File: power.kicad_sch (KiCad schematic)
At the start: 80 parts, among them IC1 STM32MP157AAB3, IC3 STC3117IJT, IC4 MCP73830T-2AAI_MYY, IC5 MT41K256M16TW-107_P, IC6 STPMIC1BPQR, IC8 STUSB1600AQTR, J1 Conn_01x04, P1 USB_C_Plug_USB2.0, Q1 PMDPB70XP_115

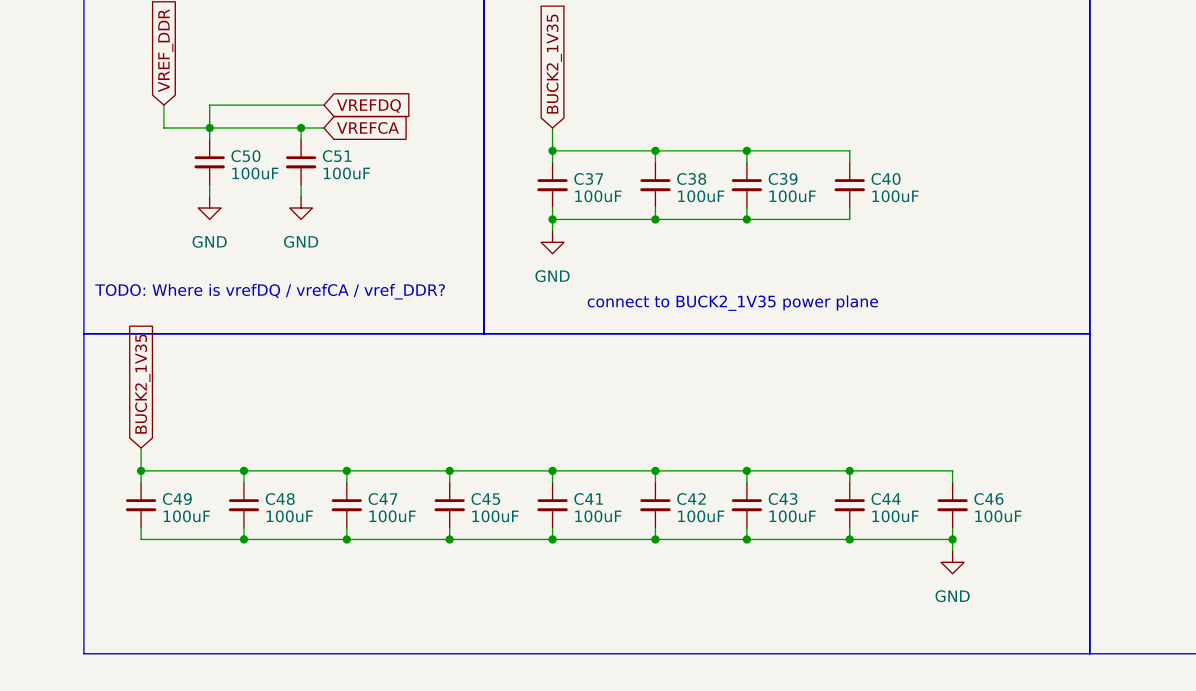
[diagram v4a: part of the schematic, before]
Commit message: added supply to nRF
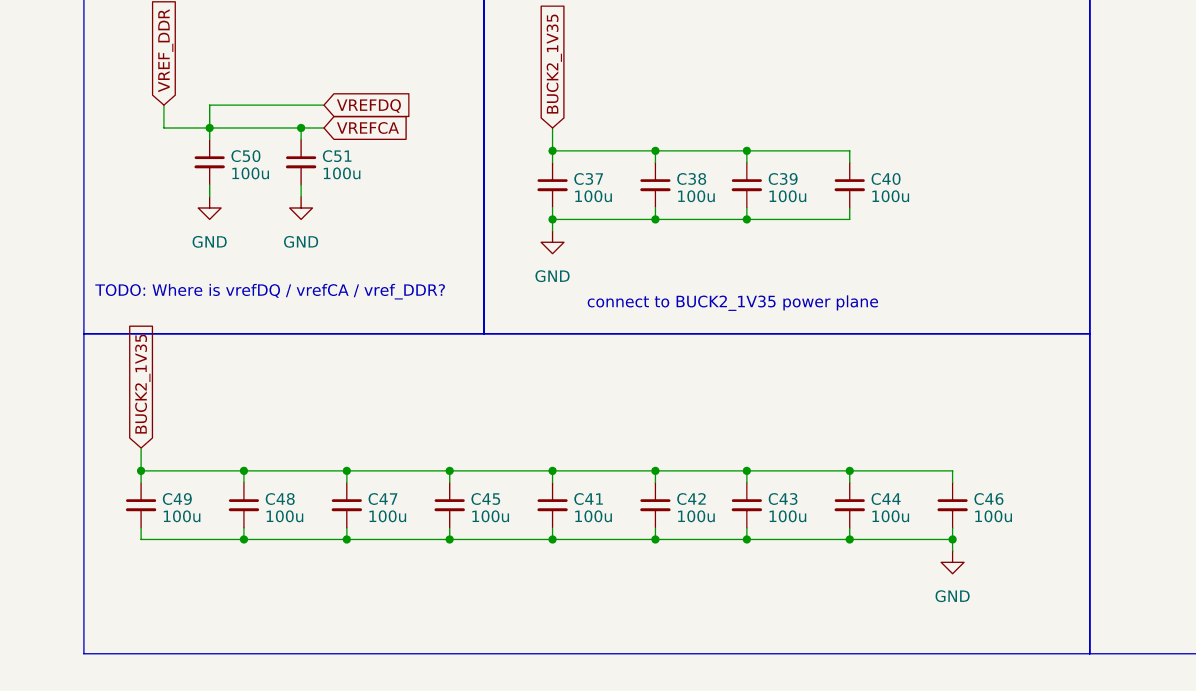
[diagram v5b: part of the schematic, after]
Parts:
- C37, C38, C39, C40, C41, C42, C43, C44, C45, C46, C47, C48, C49, C50, C51: value 100uF -> 100u
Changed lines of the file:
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@@
       (effects (font (size 1.27 1.27)) (justify left))
     )
-    (property "Value" "100uF" (at 232.1941 238.7736 0)
+    (property "Value" "100u" (at 232.1941 238.7736 0)
       (effects (font (size 1.27 1.27)) (justify left))
     )
@@
       (effects (font (size 1.27 1.27)) (justify left))
     )
-    (property "Value" "100uF" (at 220.7641 238.7736 0)
+    (property "Value" "100u" (at 220.7641 238.7736 0)
       (effects (font (size 1.27 1.27)) (justify left))
     )
@@
       (effects (font (size 1.27 1.27)) (justify left))
     )
-    (property "Value" "100uF" (at 186.4741 238.7736 0)
+    (property "Value" "100u" (at 186.4741 238.7736 0)
       (effects (font (size 1.27 1.27)) (justify left))
     )
@@
       (effects (font (size 1.27 1.27)) (justify left))
     )
-    (property "Value" "100uF" (at 253.7841 203.2136 0)
+    (property "Value" "100u" (at 253.7841 203.2136 0)
       (effects (font (size 1.27 1.27)) (justify left))
     )
@@
       (effects (font (size 1.27 1.27)) (justify left))
     )
-    (property "Value" "100uF" (at 197.9041 238.7736 0)
+    (property "Value" "100u" (at 197.9041 238.7736 0)
       (effects (font (size 1.27 1.27)) (justify left))
     )
@@
       (effects (font (size 1.27 1.27)) (justify left))
     )
-    (property "Value" "100uF" (at 243.6241 238.7736 0)
+    (property "Value" "100u" (at 243.6241 238.7736 0)
       (effects (font (size 1.27 1.27)) (justify left))
     )
@@
       (effects (font (size 1.27 1.27)) (justify left))
     )
-    (property "Value" "100uF" (at 194.0941 200.6736 0)
+    (property "Value" "100u" (at 194.0941 200.6736 0)
       (effects (font (size 1.27 1.27)) (justify left))
     )
@@
       (effects (font (size 1.27 1.27)) (justify left))
     )
-    (property "Value" "100uF" (at 265.2141 238.7736 0)
+    (property "Value" "100u" (at 265.2141 238.7736 0)
       (effects (font (size 1.27 1.27)) (justify left))
     )
@@
       (effects (font (size 1.27 1.27)) (justify left))
     )
-    (property "Value" "100uF" (at 276.6441 238.7736 0)
+    (property "Value" "100u" (at 276.6441 238.7736 0)
       (effects (font (size 1.27 1.27)) (justify left))
     )
@@
       (effects (font (size 1.27 1.27)) (justify left))
     )
-    (property "Value" "100uF" (at 209.3341 238.7736 0)
+    (property "Value" "100u" (at 209.3341 238.7736 0)
       (effects (font (size 1.27 1.27)) (justify left))
     )
@@
       (effects (font (size 1.27 1.27)) (justify left))
     )
-    (property "Value" "100uF" (at 265.2141 203.2136 0)
+    (property "Value" "100u" (at 265.2141 203.2136 0)
       (effects (font (size 1.27 1.27)) (justify left))
     )
@@
       (effects (font (size 1.27 1.27)) (justify left))
     )
-    (property "Value" "100uF" (at 253.7841 238.7736 0)
+    (property "Value" "100u" (at 253.7841 238.7736 0)
       (effects (font (size 1.27 1.27)) (justify left))
     )
@@
       (effects (font (size 1.27 1.27)) (justify left))
     )
-    (property "Value" "100uF" (at 243.6241 203.2136 0)
+    (property "Value" "100u" (at 243.6241 203.2136 0)
       (effects (font (size 1.27 1.27)) (justify left))
     )
@@
       (effects (font (size 1.27 1.27)) (justify left))
     )
-    (property "Value" "100uF" (at 204.2541 200.6736 0)
+    (property "Value" "100u" (at 204.2541 200.6736 0)
       (effects (font (size 1.27 1.27)) (justify left))
     )
@@
       (effects (font (size 1.27 1.27)) (justify left))
     )
-    (property "Value" "100uF" (at 232.1941 203.2136 0)
+    (property "Value" "100u" (at 232.1941 203.2136 0)
       (effects (font (size 1.27 1.27)) (justify left))
     )

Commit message: added decoupling capacitors to mp1
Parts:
- added C100, C101, C102, C103, C104, C105, C108, C110, C111, C115, C78, C79, C80, C81, C82, C83, C84, C85, C86, C87, C88, C89, C90, C91, C92, C93, C94, C95, C96, C99: 1u, Capacitor_SMD:C_0603_1608Metric, symbol Device:C_Small
- added C106, C107, C109: 2u2, Capacitor_SMD:C_0603_1608Metric, symbol Device:C_Small
- added C112, C116, C77: 100n, Capacitor_SMD:C_0603_1608Metric, symbol Device:C_Small
- added C97, C98: 1n, Capacitor_SMD:C_0603_1608Metric, symbol Device:C_Small
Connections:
- net BUCK1_1V2: now also C78.1, C79.1, C80.1, C81.1, C82.1, C83.1, C84.1, C85.1, C86.1, C87.1, C88.1, C89.1, C90.1, C91.1, C92.1; no longer IC1.B16 (VDD_1V2_DSI__REG)
- net BUCK2_1V35: now also C93.1, C94.1, C95.1, C96.1, C97.1, C98.1
- net BUCK4_1V8: now also C100.1, C101.1, C102.1, C103.1, C104.1, C105.1, C111.1, C112.1, C115.1, C116.1, C77.1, C99.1
- net GND: now also C100.2, C101.2, C102.2, C103.2, C104.2, C105.2, C106.2, C107.2, C108.2, C109.2, C110.2, C111.2, C112.2, C115.2, C116.2, C77.2, C78.2, C79.2, C80.2, C81.2, C82.2, C83.2, C84.2, C85.2, C86.2, C87.2, C88.2, C89.2, C90.2, C91.2, C92.2, C93.2, C94.2, C95.2, C96.2, C97.2, C98.2, C99.2
- net LDO1_1V8: now also C107.1, C108.1
- net VDD_USB renamed MP1_VDD_USB
- net MP1_VDD_USB: now also C110.1
- new net MP1_VDD1V2_DSI: C106.1, IC1.A16 (VDD1V2__DSI_PHY), IC1.B16 (VDD_1V2_DSI__REG)
- new net MP1_VDDA_1V1_REG: C109.1, IC1.W11 (VDDA_1V1_REG)
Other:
- note added: "RAM"
- note added: "VBAT"
- note added: "VDD"
- note added: "VDD1V2"
- note added: "VDDA"
- note added: "VDDA_1V1"
- note added: "VDDA_1V8"
- note added: "VDDQ_DDR"
- note added: "VDD_ANA"
- note added: "VDD_CORE"
- note added: "VDD_PLL"
- note added: "VDD_USB"
- note added: "VREF"
- note added: "VREF- must be connected to VSSA then to VSS plane"
- note added: "connect close to VSSA"
- note added: "connect close to VSSA and VREF-"
- note added: "connect close to VSS_ANA"
- note added: "connect close to VSS_PLL, VSS_PLL2"
- note added: "connect close to VSS_USBHS"
- note removed: "Caution: Datasheet P. 123 "Each power supply pair (VDD /VSS , VDDCORE/VSS, VDDA/VSSA ...) must be decoupled with filtering ceramic capacitors. These capacitors must be placed as close as possible to, or below, the appropriate pins on the underside of the PCB to ensure good operation of the device.""
- note removed: "VREF- == VSSA (== VSS?) Otherwise all GNDs can be linked together"
- moved on the sheet: C37, C38, C39, C40, C41, C42, C43, C44, C45, C46, C47, C48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

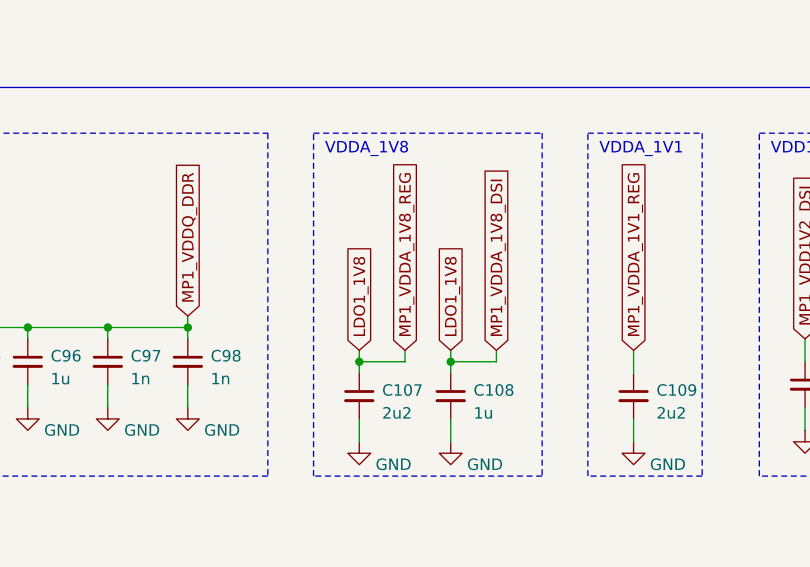
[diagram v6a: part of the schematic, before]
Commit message: fixed MP1_VDDA_1V8_REG connection
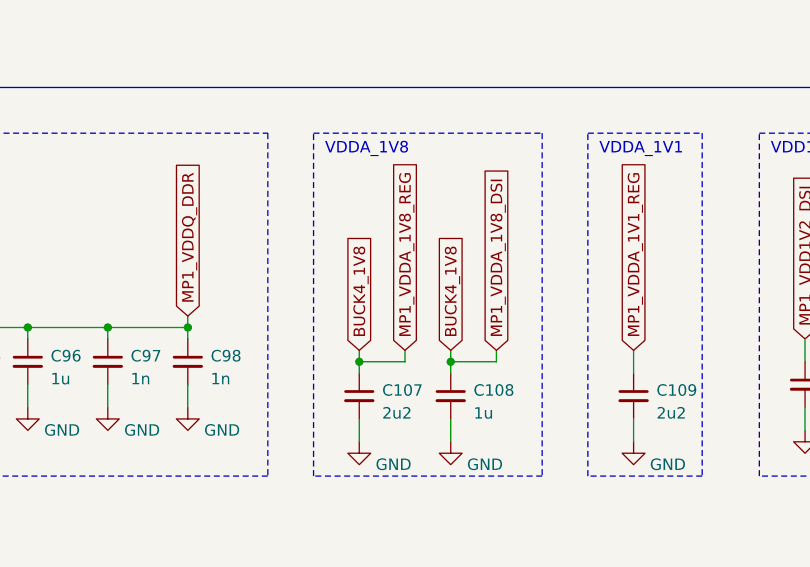
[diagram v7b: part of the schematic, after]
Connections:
- net LDO1_1V8 is gone; now on net BUCK4_1V8: C107.1, C108.1, IC1.B12 (VDDA_1V8_DSI), IC1.V11 (VDDA_1V8_REG)
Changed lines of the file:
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@@
+    )
+  )
+  (global_label "BUCK4_1V8" (shape input) (at 398.78 207.01 90) (fields_autoplaced)
+    (effects (font (size 1.27 1.27)) (justify left))
+    (property "Intersheetrefs" "${INTERSHEET_REFS}" (at 398.78 200.5966 90)
+      (effects (font (size 1.27 1.27)) (justify left) hide)
     )
   )
@@
     )
   )
-  (global_label "LDO1_1V8" (shape input) (at 398.78 207.01 90) (fields_autoplaced)
-    (effects (font (size 1.27 1.27)) (justify left))
-    (property "Intersheetrefs" "${INTERSHEET_REFS}" (at 398.78 194.7909 90)
-      (effects (font (size 1.27 1.27)) (justify left) hide)
-    )
-  )
   (global_label "SDA" (shape input) (at 280.67 111.76 180) (fields_autoplaced)
     (effects (font (size 1.27 1.27)) (justify right))
@@
     )
   )
+  (global_label "BUCK4_1V8" (shape input) (at 408.94 207.01 90) (fields_autoplaced)
+    (effects (font (size 1.27 1.27)) (justify left))
+    (property "Intersheetrefs" "${INTERSHEET_REFS}" (at 408.94 200.5966 90)
+      (effects (font (size 1.27 1.27)) (justify left) hide)
+    )
+  )
   (global_label "USB_ATTACH" (shape input) (at 176.53 104.14 0) (fields_autoplaced)
     (effects (font (size 1.27 1.27)) (justify left))
@@
       (effects (font (size 1.27 1.27)) (justify left) hide)
     )
-  )
-  (global_label "LDO1_1V8" (shape input) (at 408.94 207.01 90) (fields_autoplaced)
-    (effects (font (size 1.27 1.27)) (justify left))
-    (property "Intersheetrefs" "${INTERSHEET_REFS}" (at 408.94 194.7909 90)
-      (effects (font (size 1.27 1.27)) (justify left) hide)
-    )
